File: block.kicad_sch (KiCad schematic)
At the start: 0 parts

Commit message: Added Sheets
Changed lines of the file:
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@@
 	)
 	(rectangle
-		(start 265.43 123.19)
-		(end 254 156.21)
+		(start 254 123.19)
+		(end 265.43 156.21)
 		(stroke
 			(width -0.0001)
@@
 		(fill
 			(type color)
-			(color 227 227 227 1)
+			(color 117 117 117 1)
 		)
 	)
@@
 		(fill
 			(type color)
-			(color 255 139 147 1)
+			(color 139 243 255 1)
 		)
 	)
@@
 		(fill
 			(type color)
-			(color 255 139 147 1)
+			(color 178 255 139 1)
 		)
 	)

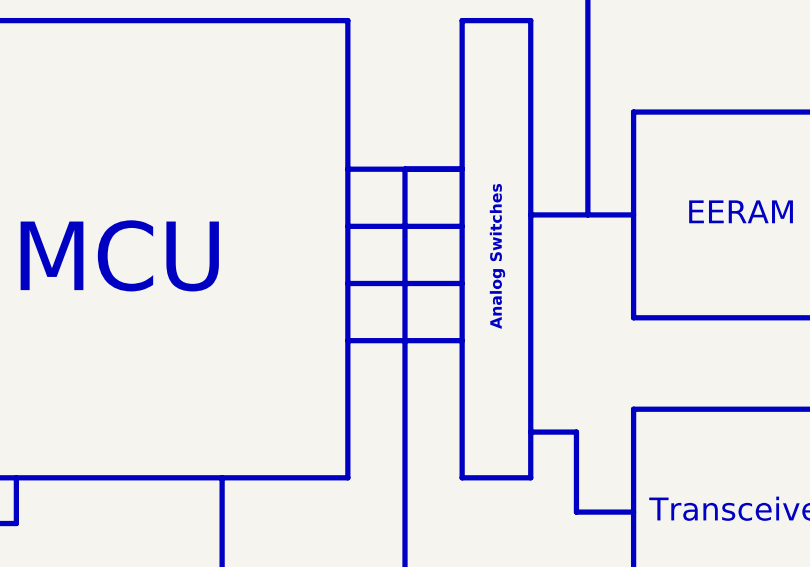
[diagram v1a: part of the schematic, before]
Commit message: Added power schematic
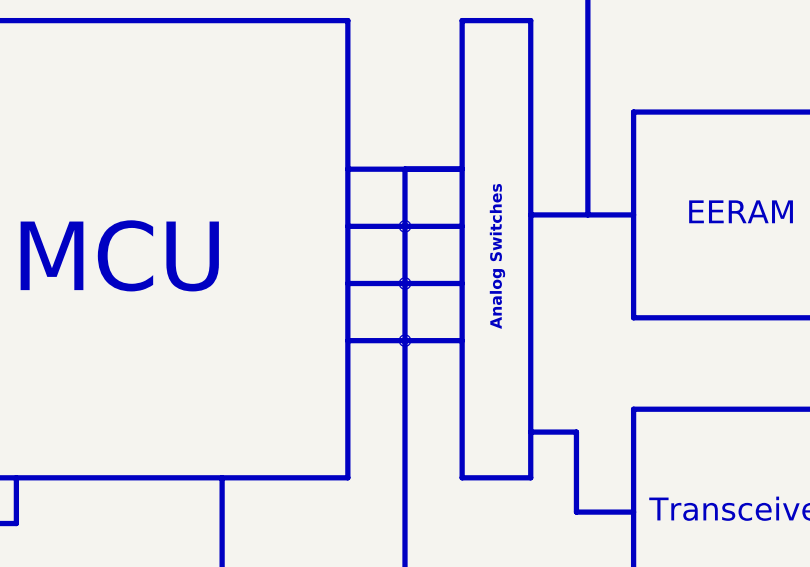
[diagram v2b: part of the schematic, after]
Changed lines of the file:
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@@
+		)
+	)
+	(circle
+		(center 168.91 99.06)
+		(radius 0.635)
+		(stroke
+			(width 0)
+			(type default)
+			(color 0 0 0 1)
+		)
+		(fill
+			(type color)
+			(color 0 0 0 1)
 		)
 	)
@@
 		)
 	)
+	(circle
+		(center 168.91 105.41)
+		(radius 0.635)
+		(stroke
+			(width 0)
+			(type default)
+			(color 0 0 0 1)
+		)
+		(fill
+			(type color)
+			(color 0 0 0 1)
+		)
+	)
 	(rectangle
 		(start 175.26 76.2)
@@
 		)
 	)
+	(circle
+		(center 168.91 111.76)
+		(radius 0.635)
+		(stroke
+			(width 0)
+			(type default)
+			(color 0 0 0 1)
+		)
+		(fill
+			(type color)
+			(color 0 0 0 1)
+		)
+	)

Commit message: Started PCB
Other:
- note removed: "Analog Switches"
